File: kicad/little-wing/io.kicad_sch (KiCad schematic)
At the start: 14 parts, among them J3 rgb, J4 columns, J6 rows, J7 sensor, Q1 AO3401A, Q2 2N7002

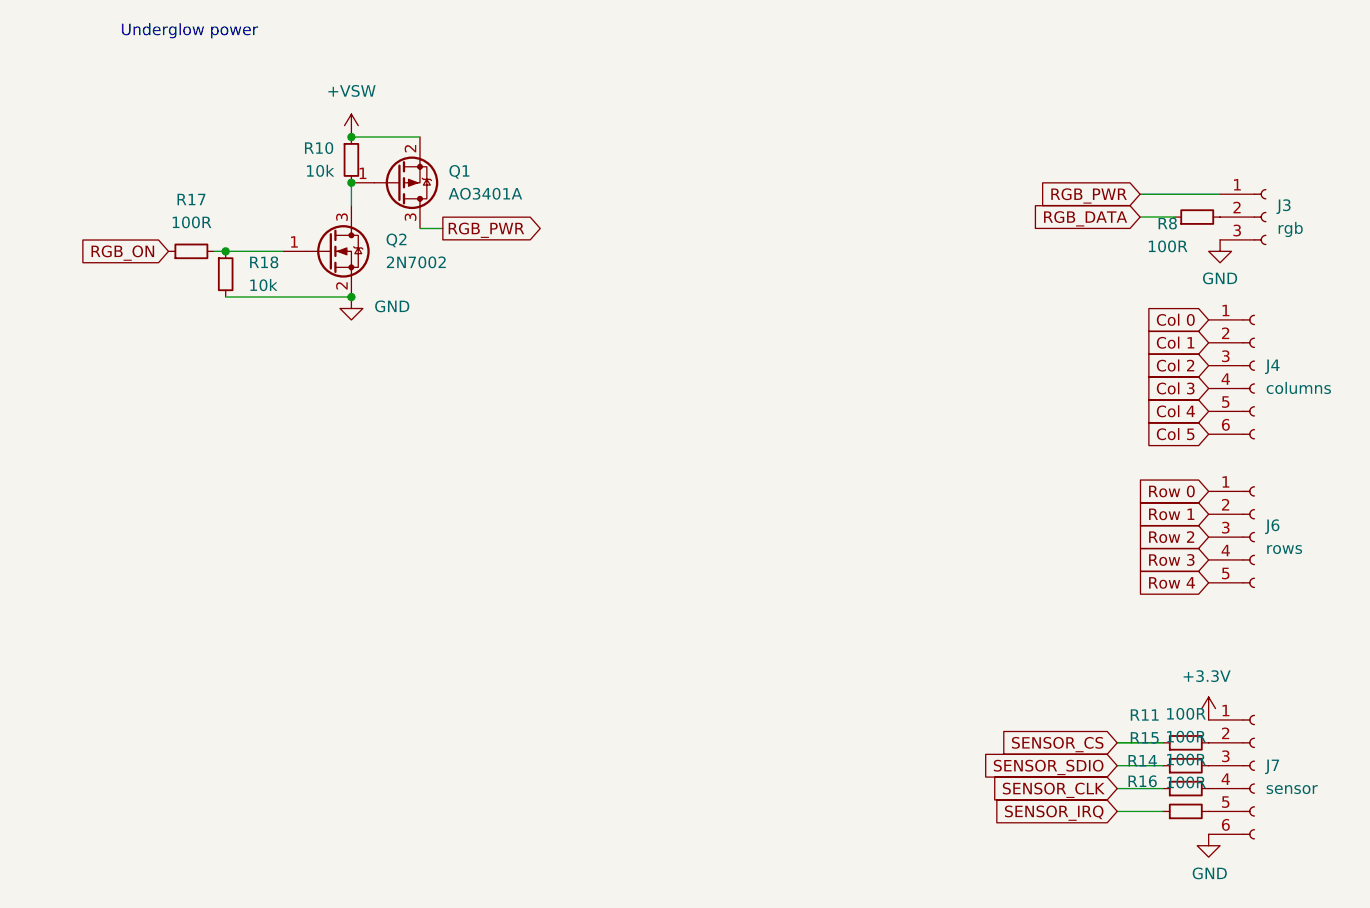
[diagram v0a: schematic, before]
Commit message: Cleaning up the schematics a bit more
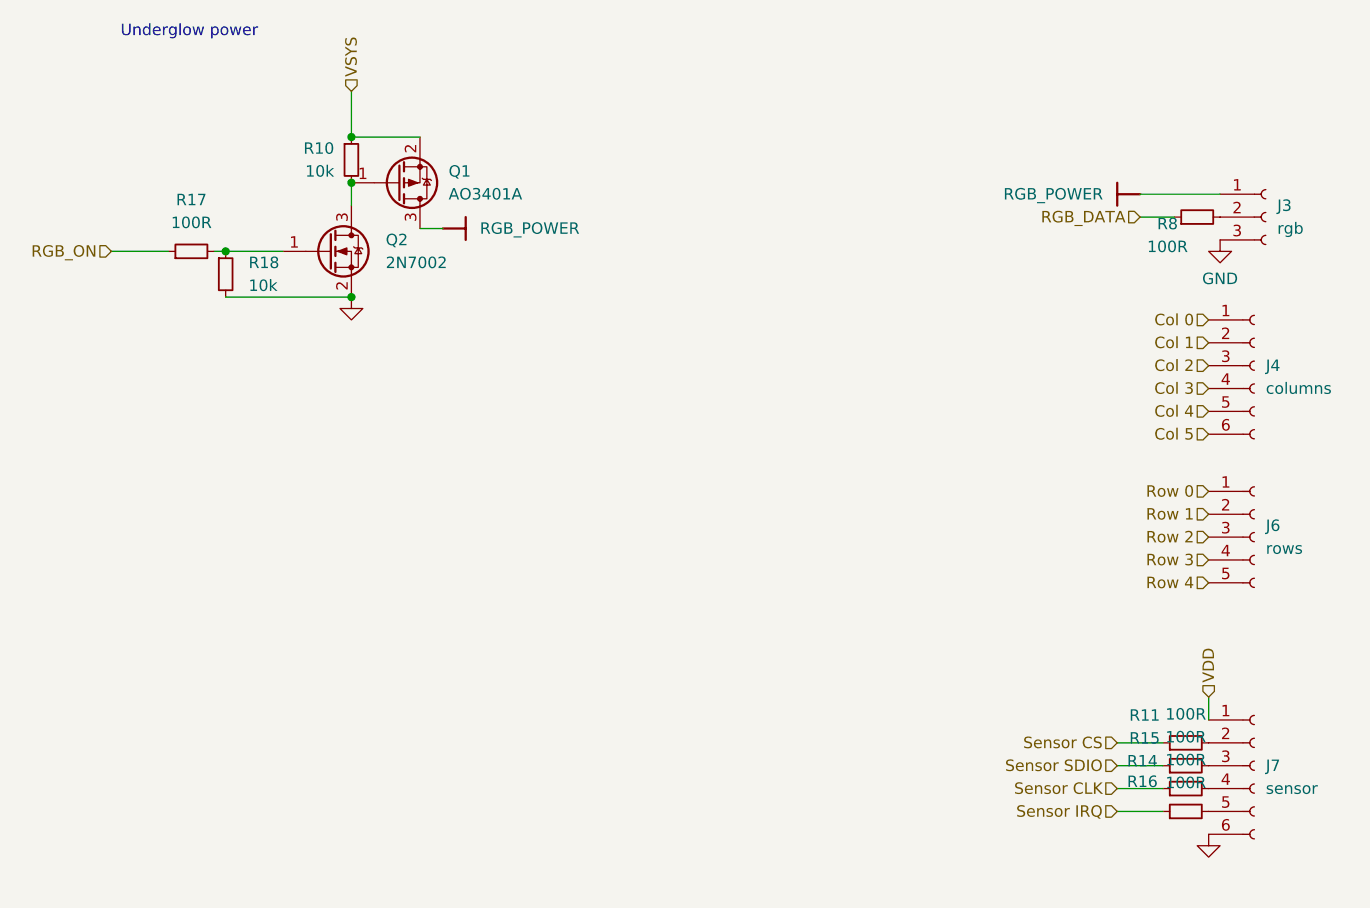
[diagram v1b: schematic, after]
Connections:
- net +3.3V renamed VDD
- net +VSW renamed VSYS
- net RGB_PWR renamed RGB_POWER
- net SENSOR_CLK renamed Sensor CLK
- net SENSOR_CS renamed Sensor CS
- net SENSOR_IRQ renamed Sensor IRQ
- net SENSOR_SDIO renamed Sensor SDIO

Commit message: Reseting all the extra components sizes
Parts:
- Q1: footprint Package_TO_SOT_SMD:SOT-23 -> Package_TO_SOT_SMD:SOT-323_SC-70
- Q2: footprint Package_TO_SOT_SMD:SOT-23 -> Package_TO_SOT_SMD:SOT-523
- R10, R11, R14, R15, R16, R17, R8: footprint Resistor_SMD:R_0402_1005Metric -> Resistor_SMD:R_0201_0603Metric
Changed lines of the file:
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@@
 			)
 		)
-		(property "Footprint" "Resistor_SMD:R_0402_1005Metric"
+		(property "Footprint" "Resistor_SMD:R_0201_0603Metric"
 			(at 177.8 50.8 0)
 			(effects
@@
 			)
 		)
-		(property "Footprint" "Package_TO_SOT_SMD:SOT-23"
+		(property "Footprint" "Package_TO_SOT_SMD:SOT-523"
 			(at 86.36 56.515 0)
 			(effects
@@
 			)
 		)
-		(property "Footprint" "Resistor_SMD:R_0402_1005Metric"
+		(property "Footprint" "Resistor_SMD:R_0201_0603Metric"
 			(at 176.53 109.22 0)
 			(effects
@@
 			)
 		)
-		(property "Footprint" "Package_TO_SOT_SMD:SOT-23"
+		(property "Footprint" "Package_TO_SOT_SMD:SOT-323_SC-70"
 			(at 93.98 45.085 0)
 			(effects
@@
 			)
 		)
-		(property "Footprint" "Resistor_SMD:R_0402_1005Metric"
+		(property "Footprint" "Resistor_SMD:R_0201_0603Metric"
 			(at 176.53 116.84 0)
 			(effects
@@
 			)
 		)
-		(property "Footprint" "Resistor_SMD:R_0402_1005Metric"
+		(property "Footprint" "Resistor_SMD:R_0201_0603Metric"
 			(at 83.82 44.45 0)
 			(effects
@@
 			)
 		)
-		(property "Footprint" "Resistor_SMD:R_0402_1005Metric"
+		(property "Footprint" "Resistor_SMD:R_0201_0603Metric"
 			(at 66.04 54.61 0)
 			(effects
@@
 			)
 		)
-		(property "Footprint" "Resistor_SMD:R_0402_1005Metric"
+		(property "Footprint" "Resistor_SMD:R_0201_0603Metric"
 			(at 176.53 111.76 0)
 			(effects
@@
 			)
 		)
-		(property "Footprint" "Resistor_SMD:R_0402_1005Metric"
+		(property "Footprint" "Resistor_SMD:R_0201_0603Metric"
 			(at 176.53 114.3 0)
 			(effects

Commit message: Swapping the crystals for smaller ones
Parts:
- R18: footprint Resistor_SMD:R_0402_1005Metric -> Resistor_SMD:R_0201_0603Metric
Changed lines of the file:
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@@
 			)
 		)
-		(property "Footprint" "Resistor_SMD:R_0402_1005Metric"
+		(property "Footprint" "Resistor_SMD:R_0201_0603Metric"
 			(at 69.85 57.15 0)
 			(effects

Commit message: Dialing in the physical package
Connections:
- net GND: now also J7.1 (Pin_1); no longer J7.6 (Pin_6)
- net VDD: now also J7.6 (Pin_6); no longer J7.1 (Pin_1)
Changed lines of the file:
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@@
+		)
+	)
+	(hierarchical_label "VDD"
+		(shape input)
+		(at 179.07 119.38 270)
+		(effects
+			(font
+				(size 1.27 1.27)
+			)
+			(justify right)
 		)
 	)
@@
 			)
 			(justify right)
-		)
-	)
-	(hierarchical_label "VDD"
-		(shape input)
-		(at 179.07 104.14 90)
-		(effects
-			(font
-				(size 1.27 1.27)
-			)
-			(justify left)
 		)
 	)
@@
 		(lib_name "GND_5")
 		(lib_id "power:GND")
-		(at 179.07 119.38 0)
+		(at 179.07 104.14 180)
 		(unit 1)
 		(exclude_from_sim no)
@@
 		(dnp no)
 		(property "Reference" "#PWR039"
-			(at 179.07 125.73 0)
+			(at 179.07 97.79 0)
 			(effects
 				(font
@@
 		)
 		(property "Value" "GND"
-			(at 179.197 123.7742 0)
+			(at 178.943 99.7458 0)
 			(effects
 				(font
@@
 		)
 		(property "Footprint" ""
-			(at 179.07 119.38 0)
+			(at 179.07 104.14 0)
 			(effects
 				(font
@@
 		)
 		(property "Datasheet" ""
-			(at 179.07 119.38 0)
+			(at 179.07 104.14 0)
 			(effects
 				(font
@@
 		)
 		(property "Description" ""
-			(at 179.07 119.38 0)
-			(effects
-				(font
+			(at 179.07 104.14 0)
+			(effects
+				(font

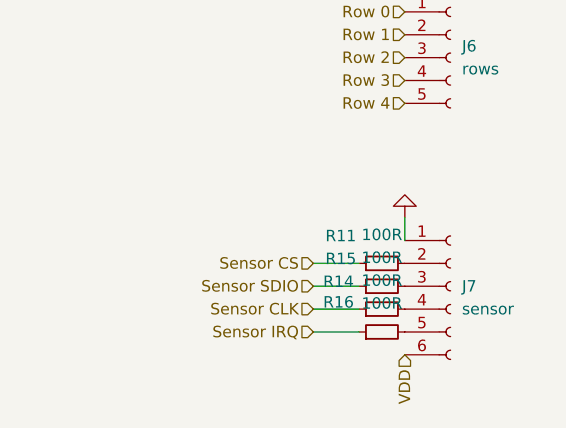
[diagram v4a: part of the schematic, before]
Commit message: Loosely attaching pins to prefiery
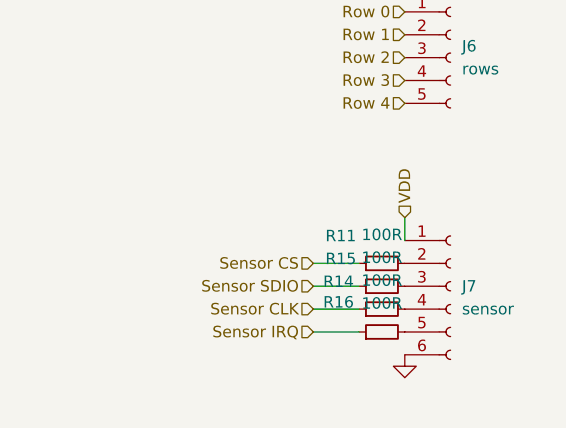
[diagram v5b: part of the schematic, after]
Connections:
- net GND: now also J7.6 (Pin_6); no longer J7.1 (Pin_1)
- net VDD: now also J7.1 (Pin_1); no longer J7.6 (Pin_6)
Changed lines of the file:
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@@
 	(hierarchical_label "VDD"
 		(shape input)
-		(at 179.07 119.38 270)
-		(effects
-			(font
-				(size 1.27 1.27)
-			)
-			(justify right)
+		(at 179.07 104.14 90)
+		(effects
+			(font
+				(size 1.27 1.27)
+			)
+			(justify left)
 		)
 	)
@@
 		(lib_name "GND_5")
 		(lib_id "power:GND")
-		(at 179.07 104.14 180)
+		(at 179.07 119.38 0)
 		(unit 1)
 		(exclude_from_sim no)
@@
 		(dnp no)
 		(property "Reference" "#PWR039"
-			(at 179.07 97.79 0)
+			(at 179.07 125.73 0)
 			(effects
 				(font
@@
 		)
 		(property "Value" "GND"
-			(at 178.943 99.7458 0)
+			(at 179.197 123.7742 0)
 			(effects
 				(font
@@
 		)
 		(property "Footprint" ""
-			(at 179.07 104.14 0)
+			(at 179.07 119.38 0)
 			(effects
 				(font
@@
 		)
 		(property "Datasheet" ""
-			(at 179.07 104.14 0)
+			(at 179.07 119.38 0)
 			(effects
 				(font
@@
 		)
 		(property "Description" ""
-			(at 179.07 104.14 0)
-			(effects
-				(font
+			(at 179.07 119.38 0)
+			(effects
+				(font

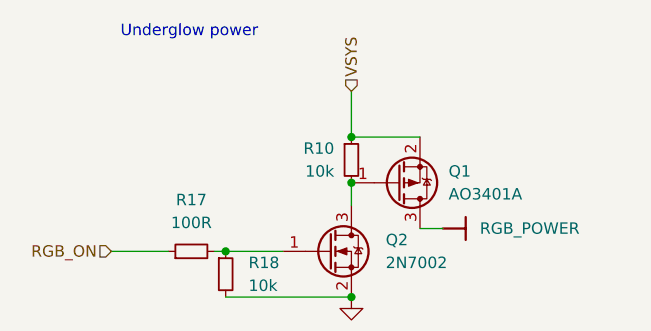
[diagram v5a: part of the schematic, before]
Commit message: Connecting remaining power lines
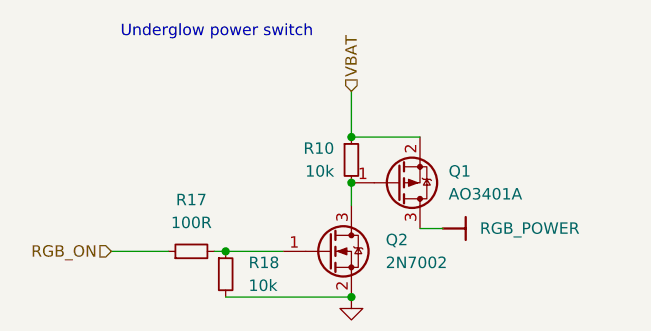
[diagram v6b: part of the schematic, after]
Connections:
- net VSYS renamed VBAT
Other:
- note added: "Underglow power switch"
- note removed: "Underglow power"
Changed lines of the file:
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@@
 	(generator_version "9.0")
 	(paper "A4")
-	(text "Underglow power"
+	(text "Underglow power switch"
 		(exclude_from_sim no)
 		(at 58.166 30.988 0)
@@
 		)
 	)
-	(hierarchical_label "VSYS"
+	(hierarchical_label "VBAT"
 		(shape input)
 		(at 83.82 36.83 90)

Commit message: Re-organising the schematics sheets a bit
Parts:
- removed J3: rgb, Connector_JST:JST_SH_SM03B-SRSS-TB_1x03-1MP_P1.00mm_Horizontal, symbol Connector:Conn_01x03_Socket
- removed J4: columns, Connector_JST:JST_SH_SM06B-SRSS-TB_1x06-1MP_P1.00mm_Horizontal, symbol Connector:Conn_01x06_Socket
- removed J6: rows, Connector_JST:JST_SH_SM05B-SRSS-TB_1x05-1MP_P1.00mm_Horizontal, symbol Connector:Conn_01x05_Socket
- removed J7: sensor, Connector_JST:JST_SH_SM06B-SRSS-TB_1x06-1MP_P1.00mm_Horizontal, symbol Connector:Conn_01x06_Socket
- removed Q1: AO3401A, Package_TO_SOT_SMD:SOT-323_SC-70, symbol Transistor_FET:AO3401A
- removed Q2: 2N7002, Package_TO_SOT_SMD:SOT-523, symbol Transistor_FET:2N7002
- removed R10, R18: 10k, Resistor_SMD:R_0201_0603Metric, symbol Device:R_Small
- removed R11, R14, R15, R16, R17, R8: 100R, Resistor_SMD:R_0201_0603Metric, symbol Device:R_Small
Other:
- note removed: "Underglow power switch"
